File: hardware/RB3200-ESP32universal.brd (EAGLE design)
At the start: 73.7 x 44.5 mm, 102 parts, among them IC1 FT232R, IC2 7805, T1 BC337, T2 BC337, U1 ESP-WROOM-32, U2 UM18533, X1 USB-MICRO-B-BOTTOM

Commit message: Add information text about license and authors
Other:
- board text added: "RB3200-ESP32universal v1.0"
- board text added: "Released under the Creative Commons Attribution-ShareAlike 4.0 License https://creativecommons.org/licenses/by-sa/4.0/ Designed by: JM & JP & JS & JV & RobotikaBrno RB3200-ESP32universal https://github.com/RoboticsBrno/RB3200-ESP32universal RobotikaBrno.cz Robotarna"
- board text removed: "ESP32 universal v1.0"
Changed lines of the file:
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@@
 <circle x="2.54" y="41.91" radius="2.54" width="0.3" layer="41"/>
 <circle x="71.12" y="41.91" radius="2.54" width="0.3" layer="41"/>
-<text x="26.035" y="1.905" size="1.4224" layer="102" font="vector" ratio="20" rot="R90">ESP32 universal v1.0</text>
+<text x="26.035" y="1.27" size="1.2" layer="102" font="vector" ratio="20" rot="R90">RB3200-ESP32universal v1.0</text>
 <text x="15.4305" y="32.3215" size="1.4" layer="102" font="vector" ratio="20">I2</text>
 <text x="15.4305" y="29.7815" size="1.4" layer="102" font="vector" ratio="20">I0</text>
@@
 <text x="28.702" y="41.91" size="1.2" layer="102" font="vector" ratio="20" rot="R270">CBS2</text>
 <text x="26.924" y="41.91" size="1.2" layer="102" font="vector" ratio="20" rot="R270">CBS4</text>
-<wire x1="-0.635" y1="0.635" x2="73.025" y2="0.635" width="0" layer="103"/>
+<wire x1="0" y1="0.635" x2="73.66" y2="0.635" width="0" layer="103"/>
 <text x="0.508" y="38.608" size="1.6764" layer="102" font="vector" ratio="16" rot="R270">5
 3
@@
 <text x="31.75" y="13.97" size="1.27" layer="16" font="vector" ratio="16" rot="MR180" align="center">Robotika
 Brno</text>
+<text x="36.83" y="-18.415" size="1.778" layer="48" font="vector" align="center">Released under the Creative Commons Attribution-ShareAlike 4.0 License
+https://creativecommons.org/licenses/by-sa/4.0/
+Designed by: JM &amp; JP &amp; JS &amp; JV &amp; RobotikaBrno
+RB3200-ESP32universal
+https://github.com/RoboticsBrno/RB3200-ESP32universal
+RobotikaBrno.cz
+Robotarna</text>
 </plain>
 <attributes>

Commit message: Publish version 2.0 of RB3200-ESP32universal and level_shifter DPS
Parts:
- removed C12: 4u7, rcl_upravena:C0805
- removed C13: 100n, rcl_upravena:C0402
- removed C14: 22u/16V, rcl_upravena:SMC_B
- removed D3: skl34, diode:SOD123
- removed IC1: FT232R, ftdichip_upravena:QFN32_LONG_PADS
- removed JP10, JP9: (no value), pinhead:2X04
- removed JP12: (no value), pinhead:1X12
- removed JP13: (no value), pinhead:1X08
- removed JP16, JP17, JP18, JP19, JP20, JP21, LED0: (no value), pinhead:1X01
- removed LED0-N, LED0-P, LED1-N, LED1-P, LED2-N, LED2-P, LED3-N, LED3-P: green, led:CHIPLED_0603
- removed LED_CBUS2, LED_CBUS3, LED_CBUS4: yellow, led:CHIP-LED0603
- added !CTS, !DCD, !DSR, !DTR, !RESET, !RTS, !SUSPEND, CHR0, CHR1, CHREN, IO0/TXLED, IO1/RXLED, IO2/RS485, IO3/WAKEUP, IO4, IO5, IO6, RI/CLK, RXD, SUSPEND, TXD: PINH1X01, pinhead_smd:1X01
- added +5V, SERVOS: (no value), pinhead:2X06
- added B1, B2: TACTM-35N-F, TACTM-35N-F:TACTM-35N-F
- added C20, C21: 100n/16V, rcl_upravena:C0402
- added C37: 330u/16V, rcl_upravena:E5-10,5
- added C67, C70: 4u7/16V, rcl_upravena:C0805
- added D5: skl34, diode:SOD123
- added EN, JP36, JP38, VUSB: (no value), pinhead:1X02
- added IC3: CP2102N-28, CP2102N:QFN28-PAD
- added LED0N, LED1N, LED2N, LED3N, LED4N, LED5N: red, led:CHIPLED_0603
- added LED0P, LED1P, LED2P, LED3P, LED4P, LED5P, LED_3V3_USB: green, led:CHIPLED_0603
- added LEDS, VCC, VCCIO: (no value), pinhead:2X03
- added R35, R50, R51: 10k, rcl_upravena:R0603
- added R36, R46, R48: 470R, rcl_upravena:R0603
- added R37: 100k, rcl_upravena:R0603
- added R47, R49: 680R, rcl_upravena:R0603
- added U3: ARDUINOR3-BPLACE, adafruit:ARDUINOR3-BPLACE
- added USB: (no value), pinhead:1X05
- C1, C6, C7: value 100n -> 100n/16V
- C10, C3, C5, C9: value 4u7 -> 4u7/16V
- C11: value 4u7 -> 100n/16V; device rcl_upravena:C0805 -> rcl_upravena:C0402
- C2, C4: value 100n -> 4u7/16V; device rcl_upravena:C0402 -> rcl_upravena:C0603
- C8: value 22u/16V -> 4u7/16V; device rcl_upravena:SMC_B -> rcl_upravena:C0805
- D1: value (none) -> skl34; device diode:MINIMELF -> diode:SOD123
- JP11: device pinhead:1X14 -> pinhead:1X08
- LED1, LED2, LED3: value (none) -> yellow; device pinhead:1X01 -> led:CHIP-LED0603
- R1, R2, R26, R3, R38, R40, R42, R44: value 180R -> 470R
- R39, R41, R43, R45: value 180R -> 680R
- moved C8 49.4 mm to (10.2, 44.5), turned to 90 degrees
- moved C10 42.0 mm to (5.08, 44.5), turned to 90 degrees
- moved C11 41.4 mm to (59.1, 1.75), turned to 180 degrees
- moved C9 36.9 mm to (7.62, 44.5), turned to 90 degrees
- moved C6 31.7 mm to (79.4, 1.75), flipped to the bottom, turned to 0 degrees
- moved LED3 27.7 mm to (49.5, 50.3), turned to 180 degrees
- moved JP11 22.7 mm to (40.6, 29.2), turned to 180 degrees
- moved R3 22.0 mm to (49.5, 47.0), flipped to the top, turned to 90 degrees
- moved LED1 22.0 mm to (33.0, 50.3), turned to 180 degrees
- moved D1 21.7 mm to (58.6, 47.0), flipped to the top, turned to 180 degrees
- moved LED2 19.3 mm to (34.9, 50.3), turned to 180 degrees
- moved C5 18.3 mm to (58.9, 36.0), turned to 180 degrees
- moved LED_3V3 17.2 mm to (66.5, 50.3), turned to 0 degrees
- moved U2 17.2 mm to (59.4, 39.2)
- moved C1 16.9 mm to (42.2, 41.0), flipped to the top, turned to 180 degrees
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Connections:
- net LED renamed LED_3V3
- removed net !CTS: IC1.8, JP17.1
- removed net !DCD: IC1.7, JP19.1
- removed net !DSR: IC1.6, JP18.1
- removed net !RI: IC1.3, JP20.1
- removed net 3V3_FTDI: C2.1, IC1.16
- removed net 5V->3V3: C14.+, C4.1, D2.C, U2.P$1, U2.P$3
- removed net CBUS0: IC1.22, JP16.1
- removed net CBUS1: IC1.21, JP21.1
- removed net CBUS2: IC1.10, R1.2
- removed net CBUS2_LED: LED_CBUS2.C, R1.1
- removed net CBUS3: IC1.11, R2.2
- removed net CBUS3_LED: LED_CBUS3.C, R2.1
- removed net CBUS4: IC1.9, R3.2
- removed net CBUS4_LED: LED_CBUS4.C, R3.1
- removed net LED0: LED0.1, R38.1, R39.1
- removed net LED0-N: LED0-N.C, R39.2
- removed net LED0-P: LED0-P.A, R38.2
- removed net LED1: LED1.1, R40.1, R41.1
- removed net LED1-N: LED1-N.C, R41.2
- removed net LED1-P: LED1-P.A, R40.2
- removed net LED2: LED2.1, R42.1, R43.1
- removed net LED2-N: LED2-N.C, R43.2
- removed net LED2-P: LED2-P.A, R42.2
- removed net LED3-N: LED3-N.C, R45.2
- removed net LED3-P: LED3-P.A, R44.2
- removed net N$10: JP2.5, JP2.6, JP3.6, R7.1
- removed net N$11: JP2.3, JP2.4, JP3.4, R6.1
- removed net N$12: JP2.1, JP2.2, JP3.2, R19.1
- removed net N$13: JP6.25, JP6.26, JP7.25, R32.1
- removed net N$14: JP6.23, JP6.24, JP7.23, R31.1
- removed net N$15: JP6.21, JP6.22, JP7.21, R30.1
- removed net N$16: JP6.19, JP6.20, JP7.19, R29.1
- removed net N$17: JP6.17, JP6.18, JP7.17, R28.1
- removed net N$18: JP6.15, JP6.16, JP7.15, R27.1
- removed net N$19: JP6.13, JP6.14, JP7.13, R25.1
- removed net N$20: JP6.11, JP6.12, JP7.11, R24.1
- removed net N$21: JP6.10, JP6.9, JP7.9, R23.1
- removed net N$23: JP6.5, JP6.6, JP7.5, R21.1
- removed net N$24: JP6.3, JP6.4, JP7.3, R20.1
- removed net N$25: JP10.1, JP10.2
- removed net N$26: JP6.1, JP6.2, JP7.1, R22.1
- removed net N$27: JP6.7, JP6.8, JP7.7, R33.1
- removed net N$28: JP6.27, JP6.28, JP7.27, R34.1
- removed net N$29: JP10.3, JP10.4
- removed net N$30: JP10.5, JP10.6
- removed net N$5: JP2.15, JP2.16, JP3.16, R14.1
- removed net N$6: JP2.13, JP2.14, JP3.14, R13.1
- removed net N$7: JP2.11, JP2.12, JP3.12, R10.1
- removed net N$8: JP2.10, JP2.9, JP3.10, R9.1
- removed net N$9: JP2.7, JP2.8, JP3.8, R8.1
- removed net USBDM: IC1.15, X1.2
- removed net USBDP: IC1.14, X1.3
- new net !RESET: !RESET.1, IC3.9, R35.1
- new net !SHDN: JP36.2, R37.2, U2.P$3
- new net !SUSPEND: !SUSPEND.1, IC3.11
- new net 3V3_IN: C37.+, C4.1, D1.C, R37.1, U2.P$1
- new net 5V_USB: D2.C, VUSB.1
- new net BTN0: B1.P$4, C6.2, JP38.1, R51.1
- new net BTN1: B2.P$4, C11.2, JP38.2, R50.1
- new net CHR0: CHR0.1, IC3.15
- new net CHR1: CHR1.1, IC3.14
- new net CHREN: CHREN.1, IC3.13
- new net CLK/!RI: IC3.2, RI/CLK.1
- new net DCD: !DCD.1, IC3.1
- new net DM: IC3.5, USB.2, X1.2
- new net DP: IC3.4, USB.3, X1.3
- new net DSR: !DSR.1, IC3.27
- new net IO0_!RST!_: JP5.12, R31.2, T2.3, U1.25
- new net IO12_: JP1.11, R17.2, U1.14, U3.A2
- new net IO13_: JP1.12, R18.2, U1.16, U3.A0
- new net IO14_: JP1.10, R16.2, U1.13, U3.A1
- new net IO15_: JP5.14, R34.2, U1.23
- new net IO16_: JP5.10, R29.2, U1.27
- new net IO17_: JP5.9, R28.2, U1.28
- new net IO18_: JP5.7, R25.2, U1.30
- new net IO19_: JP5.6, R24.2, U1.31
- new net IO21_: JP5.5, R23.2, U1.33
- new net IO22_: JP5.2, R20.2, U1.36
- new net IO23_: JP5.1, R22.2, U1.37
- new net IO25_: JP1.7, R13.2, U1.10, U3.A5, U3.SCL
- new net IO26_: JP1.8, R14.2, U1.11, U3.A4, U3.SDA
- new net IO27_: JP1.9, R15.2, U1.12, U3.A3
- new net IO2_: JP5.13, R32.2, U1.24
- new net IO32_: JP1.5, R9.2, U1.8
- new net IO33_: JP1.6, R10.2, U1.9
- new net IO34_: JP1.3, R7.2, U1.6, U3.AREF
- new net IO35_: JP1.4, R8.2, U1.7
- new net IO4_: JP5.11, R30.2, U1.26
- new net IO5_: JP5.8, R27.2, U1.29
- new net LED0N: LED0N.C, R49.2
- new net LED0P: LED0P.A, R48.2
- new net LED1N: LED1N.C, R43.2
- new net LED1P: LED1P.A, R42.2
- new net LED2N: LED2N.C, R47.2
- new net LED2P: LED2P.A, R46.2
- new net LED3N: LED3N.C, R41.2
- new net LED3P: LED3P.A, R40.2
- new net LED4N: LED4N.C, R45.2
- new net LED4P: LED4P.A, R44.2
- new net LED5N: LED5N.C, R39.2
- new net LED5P: LED5P.A, R38.2
- new net LED_0: LEDS.6, R48.1, R49.1
- new net LED_1: LEDS.5, R42.1, R43.1
- new net LED_2: LEDS.4, R46.1, R47.1
- new net LED_3: LEDS.3, R40.1, R41.1
- new net LED_3V3_USB: LED_3V3_USB.C, R36.2
- new net LED_4: LEDS.2, R44.1, R45.1
- new net LED_5: LEDS.1, R38.1, R39.1
- new net N$32: SERVOS.3, SERVOS.4
- new net N$34: SERVOS.7, SERVOS.8
- new net N$36: SERVOS.11, SERVOS.12
- new net RX-LED: LED2.C, R2.1
- new net RXD0_: JP5.4, R11.2, R33.2, U1.34
- new net RX_LED: IC3.18, IO1/RXLED.1, R2.2
- new net SENSOR_VN_: JP1.2, R6.2, U1.5
- new net SENSOR_VP_: JP1.1, R19.2, U1.4
- new net SUSPEND: IC3.12, R3.1, SUSPEND.1
- new net TX-LED: LED1.C, R1.1
- new net TXD0_: JP5.3, R12.2, R21.2, U1.35
- new net TX_LED: IC3.19, IO0/TXLED.1, R1.2
- new net USBID: USB.4, X1.4
- new net USBIO3_RS485: IC3.17, IO2/RS485.1
- new net USBIO3_WAKEUP: IC3.16, IO3/WAKEUP.1
- new net USBIO4: IC3.22, IO4.1
- new net USBIO5: IC3.21, IO5.1
- new net USBIO6: IC3.20, IO6.1
- new net VCCIO: C1.1, C2.1, IC3.6, LED1.A, LED2.A, LED3.A, LED_3V3_USB.A, R35.2, VCCIO.2, VCCIO.4, VCCIO.6
- new net VUSB: C3.1, C7.1, D2.A, IC3.7, IC3.8, USB.1, X1.1
- net !DTR: now also !DTR.1, IC3.28; no longer IC1.31
- net !RTS: now also !RTS.1, IC3.24; no longer IC1.32
- net +3V3: now also JP11.8, LED0N.A, LED1N.A, LED2N.A, LED3N.A, LED4N.A, LED5N.A, PWR_1.10, PWR_1.12, PWR_1.14, PWR_1.16, PWR_1.18, PWR_1.2, PWR_1.20, PWR_1.22, PWR_1.24, PWR_1.4, PWR_1.6, PWR_1.8, PWR_2.10, PWR_2.12, PWR_2.14, PWR_2.16, PWR_2.18, PWR_2.2, PWR_2.20, PWR_2.22, PWR_2.24, PWR_2.26, PWR_2.28, PWR_2.4, PWR_2.6, PWR_2.8, R50.2, R51.2, U3.3V, U3.IOREF; no longer C1.1, C6.2, IC1.1, LED0-N.A, LED1-N.A, LED2-N.A, LED3-N.A, LED_CBUS2.A, LED_CBUS3.A, LED_CBUS4.A, PWR_1.1, PWR_1.11, PWR_1.13, PWR_1.15, PWR_1.17, PWR_1.19, PWR_1.21, PWR_1.23, PWR_1.3, PWR_1.5, PWR_1.7, PWR_1.9, PWR_2.1, PWR_2.11, PWR_2.13, PWR_2.15, PWR_2.17, PWR_2.19, PWR_2.21, PWR_2.23, PWR_2.25, PWR_2.27, PWR_2.3, PWR_2.5, PWR_2.7, PWR_2.9
- net +5V: now also +5V.1, +5V.11, +5V.3, +5V.5, +5V.7, +5V.9, C10.1, C20.1, C67.1, C70.1, C8.1, C9.1, D1.A, PWR_1.1, PWR_1.11, PWR_1.13, PWR_1.15, PWR_1.17, PWR_1.19, PWR_1.21, PWR_1.23, PWR_1.3, PWR_1.5, PWR_1.7, PWR_1.9, PWR_2.1, PWR_2.11, PWR_2.13, PWR_2.15, PWR_2.17, PWR_2.19, PWR_2.21, PWR_2.23, PWR_2.25, PWR_2.27, PWR_2.3, PWR_2.5, PWR_2.7, PWR_2.9, U3.5V, VUSB.2; no longer C10.2, C11.2, C12.2, C8.+, C9.2, D1.C, D2.A, JP9.2, JP9.4, JP9.6, JP9.8, PWR_1.10, PWR_1.12, PWR_1.14, PWR_1.16, PWR_1.18, PWR_1.2, PWR_1.20, PWR_1.22, PWR_1.24, PWR_1.4, PWR_1.6, PWR_1.8, PWR_2.10, PWR_2.12, PWR_2.14, PWR_2.16, PWR_2.18, PWR_2.2, PWR_2.20, PWR_2.22, PWR_2.24, PWR_2.26, PWR_2.28, PWR_2.4, PWR_2.6, PWR_2.8
- net EN: now also EN.1, U3.RESET; no longer JP13.2
- net GND: now also +5V.10, +5V.12, +5V.2, +5V.4, +5V.6, +5V.8, B1.P$2, B2.P$2, C10.2, C20.2, C21.2, C37.-, C67.2, C70.2, C8.2, C9.2, EN.2, IC3.3, IC3.PAD, JP11.7, JP36.1, LED0P.C, LED1P.C, LED2P.C, LED3P.C, LED4P.C, LED5P.C, R36.1, U3.GND, U3.GND1, U3.GND2, USB.5, VCC.1, VCC.3, VCC.5, VCCIO.1, VCCIO.3, VCCIO.5; no longer C10.1, C12.1, C13.2, C14.-, C8.-, C9.1, IC1.17, IC1.20, IC1.24, IC1.26, IC1.4, JP13.1, JP9.1, JP9.3, JP9.5, JP9.7, LED0-P.C, LED1-P.C, LED2-P.C, LED3-P.C
- net IO0_!RST: now also JP6.23, JP6.24, JP7.23, R31.1, U3.D6; no longer JP11.12, JP5.12, R31.2, T2.3, U1.25
- net IO12: now also JP2.21, JP2.22, JP3.22, R17.1; no longer JP1.11, JP12.11, R17.2, U1.14
- net IO13: now also JP2.23, JP2.24, JP3.24, R18.1; no longer JP1.12, JP12.12, R18.2, U1.16
- net IO14: now also JP2.19, JP2.20, JP3.20, R16.1; no longer JP1.10, JP12.10, R16.2, U1.13
- net IO15: now also JP6.27, JP6.28, JP7.27, R34.1, U3.D4; no longer JP11.14, JP5.14, R34.2, U1.23
- net IO16: now also JP6.19, JP6.20, JP7.19, R29.1, U3.D8; no longer JP11.10, JP5.10, R29.2, U1.27
- net IO17: now also JP6.17, JP6.18, JP7.17, R28.1, U3.D9; no longer JP11.9, JP5.9, R28.2, U1.28
- net IO18: now also JP6.13, JP6.14, JP7.13, R25.1, U3.D11; no longer JP11.7, JP5.7, R25.2, U1.30
- net IO19: now also JP6.11, JP6.12, JP7.11, R24.1, U3.D12; no longer JP11.6, JP5.6, R24.2, U1.31
- net IO2: now also JP6.25, JP6.26, JP7.25, R32.1, U3.D5; no longer JP11.13, JP5.13, R32.2, U1.24
- net IO21: now also JP6.10, JP6.9, JP7.9, R23.1, U3.D13; no longer JP11.5, JP5.5, R23.2, U1.33
- net IO22: now also JP6.3, JP6.4, JP7.3, R20.1, U3.D3; no longer JP11.2, JP5.2, R20.2, U1.36
- net IO23: now also JP6.1, JP6.2, JP7.1, R22.1, U3.D2; no longer JP11.1, JP5.1, R22.2, U1.37
- net IO25: now also JP2.13, JP2.14, JP3.14, R13.1; no longer JP1.7, JP12.7, R13.2, U1.10
- net IO26: now also JP2.15, JP2.16, JP3.16, R14.1; no longer JP1.8, JP12.8, R14.2, U1.11
- net IO27: now also JP2.17, JP2.18, JP3.18, R15.1; no longer JP1.9, JP12.9, R15.2, U1.12
- net IO32: now also JP2.10, JP2.9, JP3.10, R9.1; no longer JP1.5, JP12.5, R9.2, U1.8
- net IO33: now also JP2.11, JP2.12, JP3.12, R10.1; no longer JP1.6, JP12.6, R10.2, U1.9
- net IO34: now also JP2.5, JP2.6, JP3.6, R7.1; no longer JP1.3, JP12.3, R7.2, U1.6
- net IO35: now also JP2.7, JP2.8, JP3.8, R8.1; no longer JP1.4, JP12.4, R8.2, U1.7
- net IO4: now also JP6.21, JP6.22, JP7.21, R30.1, U3.D7; no longer JP11.11, JP5.11, R30.2, U1.26
- net IO5: now also JP6.15, JP6.16, JP7.15, R27.1, U3.D10; no longer JP11.8, JP5.8, R27.2, U1.29
- net N$1: now also U3.RESERVED; no longer JP2.23, JP2.24, JP3.24, R18.1
- net N$2: now also !CTS.1, IC3.23; no longer JP2.21, JP2.22, JP3.22, R17.1
- net N$3: now also U3.VIN; no longer JP2.19, JP2.20, JP3.20, R16.1
- net N$31: now also SERVOS.1, SERVOS.2; no longer JP10.7, JP10.8
- net N$33: now also SERVOS.5, SERVOS.6; no longer C3.1, C7.1, D1.A, IC1.19, X1.1
- net N$35: now also SERVOS.10, SERVOS.9; no longer LED3.1, R44.1, R45.1
- net N$4: now also LED3.C, R3.2; no longer JP2.17, JP2.18, JP3.18, R15.1
- net NC-CS: now also JP11.3; no longer JP13.5
- net NC-HOLD: now also JP11.1; no longer JP13.3
- net NC-MISO: now also JP11.6; no longer JP13.8
- net NC-MOSI: now also JP11.5; no longer JP13.7
- net NC-SCK: now also JP11.4; no longer JP13.6
- net NC-WP: now also JP11.2; no longer JP13.4
- net RXD: now also IC3.25, RXD.1; no longer IC1.2
- net RXD0: now also JP6.7, JP6.8, JP7.7, R33.1, U3.D0; no longer JP11.4, JP5.4, R11.2, R33.2, U1.34
- net SENSOR_VN: now also JP2.3, JP2.4, JP3.4, R6.1; no longer JP1.2, JP12.2, R6.2, U1.5
- net SENSOR_VP: now also JP2.1, JP2.2, JP3.2, R19.1; no longer JP1.1, JP12.1, R19.2, U1.4
- net TXD: now also IC3.26, TXD.1; no longer IC1.30
- net TXD0: now also JP6.5, JP6.6, JP7.5, R21.1, U3.D1; no longer JP11.3, JP5.3, R12.2, R21.2, U1.35
- net VCC: now also D5.A, VCC.2, VCC.4, VCC.6; no longer D3.A
- net VCC->5V: now also C21.1, D5.C; no longer C13.1, D3.C
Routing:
- net GND: track 70.4 -> 233.2 mm, vias 61 -> 32
- net IO25_: track 0.00 -> 106.0 mm
- net IO26_: track 0.00 -> 99.1 mm
- net EN: track 42.3 -> 104.2 mm, vias 4 -> 1
- net VCCIO: track 0.00 -> 58.6 mm, vias 0 -> 3
- net IO34_: track 0.00 -> 54.6 mm, vias 0 -> 1
- net IO23: track 10.4 -> 58.5 mm
- net IO22: track 9.84 -> 52.2 mm
- net IO27_: track 0.00 -> 38.4 mm
- net TXD0_: track 0.00 -> 38.0 mm
- net TX_LED: track 0.00 -> 32.8 mm
- net RX_LED: track 0.00 -> 28.6 mm
- net RXD0_: track 0.00 -> 26.9 mm
- net IO12_: track 0.00 -> 25.5 mm
- net IO14_: track 0.00 -> 25.0 mm
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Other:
- board size 73.7 x 44.5 mm -> 83.8 x 52.1 mm
- board text added: "!SHDN"
- board text added: "+ -"
- board text added: "0"
- board text added: "1"
- board text added: "2"
- board text added: "3"
- board text added: "4"
- board text added: "4 2 0"
- board text added: "5"
- board text added: "5 3 1"
- board text added: "5V_USB"
- board text added: "G 5 S S"
- board text added: "IO0"
- board text added: "IO12"
- board text added: "IO13"
- board text added: "IO14"
- board text added: "IO15"
- board text added: "IO16"
- board text added: "IO17"
- board text added: "IO18"
- board text added: "IO19"
- board text added: "IO2"
- board text added: "IO21"
- board text added: "IO22"
- board text added: "IO23"
- board text added: "IO25"
- board text added: "IO26"
- board text added: "IO27"
- board text added: "IO32"
- board text added: "IO33"
- board text added: "IO34"
- board text added: "IO35"
- board text added: "IO4"
- board text added: "LED_3V3"
- board text added: "LED_3V3_USB"
- board text added: "RB 3-17"
- board text added: "RB3200-ESP32universal v2.0"
- board text added: "ROBOTARNA"
- board text added: "RX"
- board text added: "TX"
- board text added: "github:roboticsbrno/ RB3200-ESP32universal CC BY-SA 4.0"
- board text removed: "!CTS"
- board text removed: "!DCD"
- board text removed: "!DSR"
- board text removed: "!RI"
- board text removed: "CBS0"
- board text removed: "CBS1"
- board text removed: "CBS2"
- board text removed: "CBS3"
- board text removed: "CBS4"
- board text removed: "CC BY-SA 4.0 github:roboticsbrno/ RB3200-ESP32universal"
- board text removed: "E"
- board text removed: "I0"
- board text removed: "I12"
- board text removed: "I13"
- board text removed: "I14"
- board text removed: "I15"
- board text removed: "I16"
- board text removed: "I17"
- board text removed: "I18"
- board text removed: "I19"
- board text removed: "I2"
- board text removed: "I21"
- board text removed: "I22"
- board text removed: "I23"
- board text removed: "I25"
- board text removed: "I26"
- board text removed: "I27"
- board text removed: "I32"
- board text removed: "I33"
- board text removed: "I34"
- board text removed: "I35"
- board text removed: "I4"
- board text removed: "L_3V"
- board text removed: "RB3200-ESP32universal v1.0"
- board text removed: "ROBOTARNA 3-17"
- board text removed: "Robotika Brno"

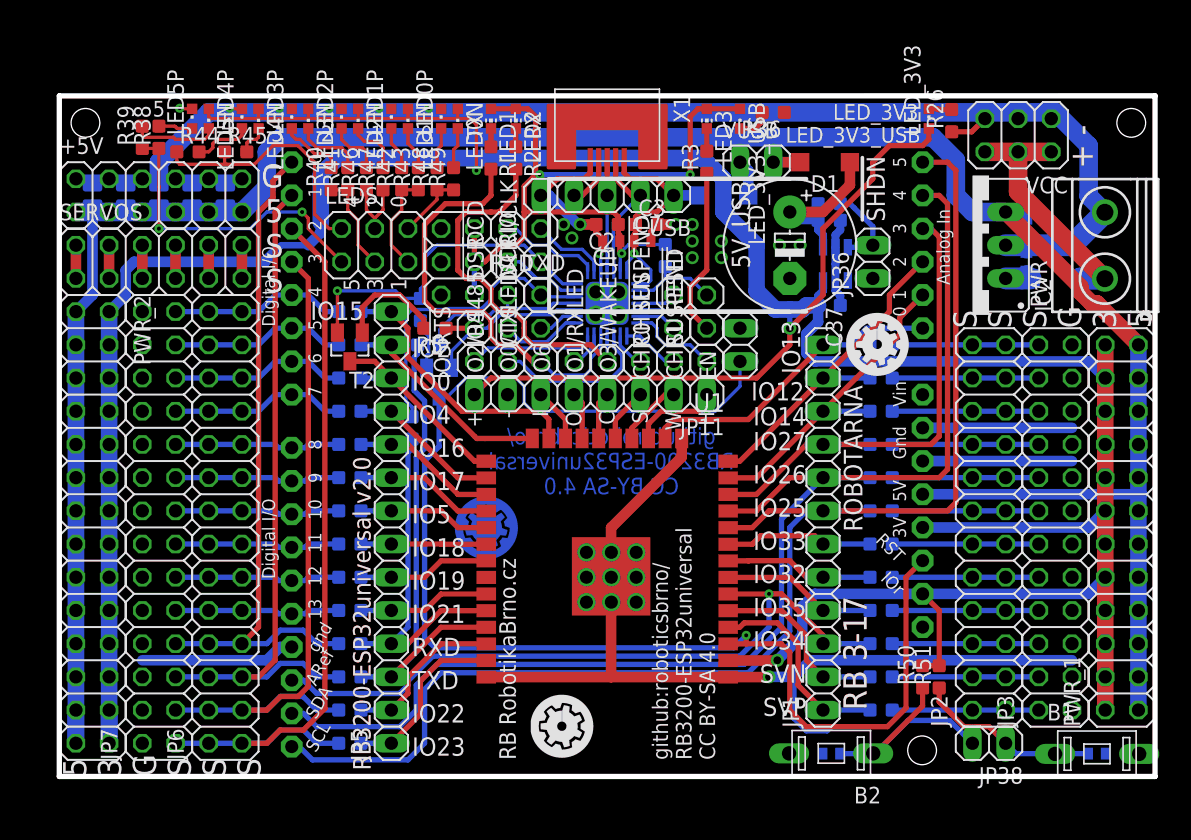
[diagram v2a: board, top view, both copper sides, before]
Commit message: updated silkscreen (and added bSilk)
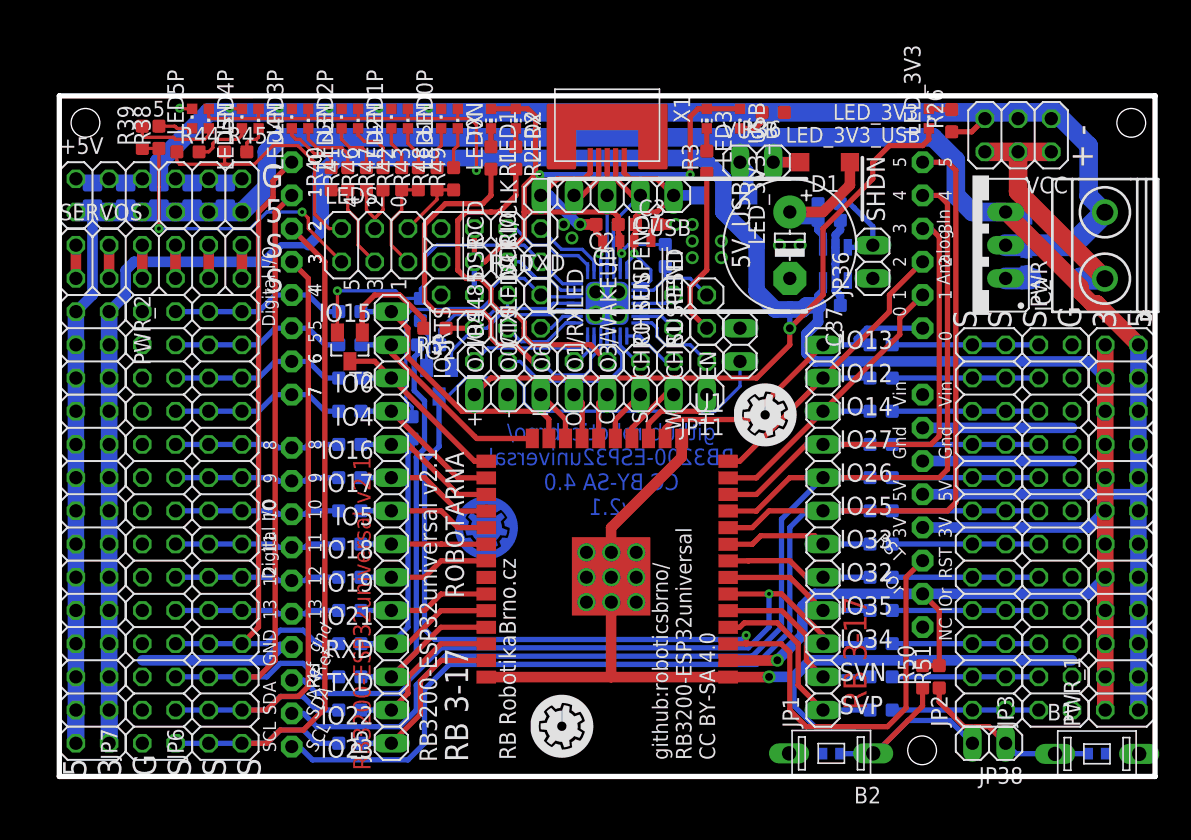
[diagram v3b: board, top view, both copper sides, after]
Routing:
- net EN: track 104.2 -> 103.3 mm
- net GND: track 233.2 -> 232.4 mm
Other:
- board text added: "10"
- board text added: "11"
- board text added: "12"
- board text added: "13"
- board text added: "3V"
- board text added: "5V"
- board text added: "6"
- board text added: "7"
- board text added: "8"
- board text added: "9"
- board text added: "ARef"
- board text added: "GND"
- board text added: "Gnd"
- board text added: "IOr"
- board text added: "NC"
- board text added: "RB RobotikaBrno.cz github:roboticsbrno/ RB3200-ESP32universal v2.1 CC BY-SA 4.0"
- board text added: "RB3200-ESP32universal v2.1"
- board text added: "RST"
- board text added: "SCL"
- board text added: "SDA"
- board text added: "Vin"
- board text added: "github:roboticsbrno/ RB3200-ESP32universal CC BY-SA 4.0 v2.1"
- board text removed: "RB3200-ESP32universal v2.0"
